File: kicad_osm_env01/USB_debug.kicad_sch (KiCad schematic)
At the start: 39 parts, among them J3 USB_B_Micro, Q2 SS8050, Q3 SS8050, U13 CP2102N-A02-GQFN24, U15 M74VHC1GT14DFT2G, U5 SP3003-02JTG

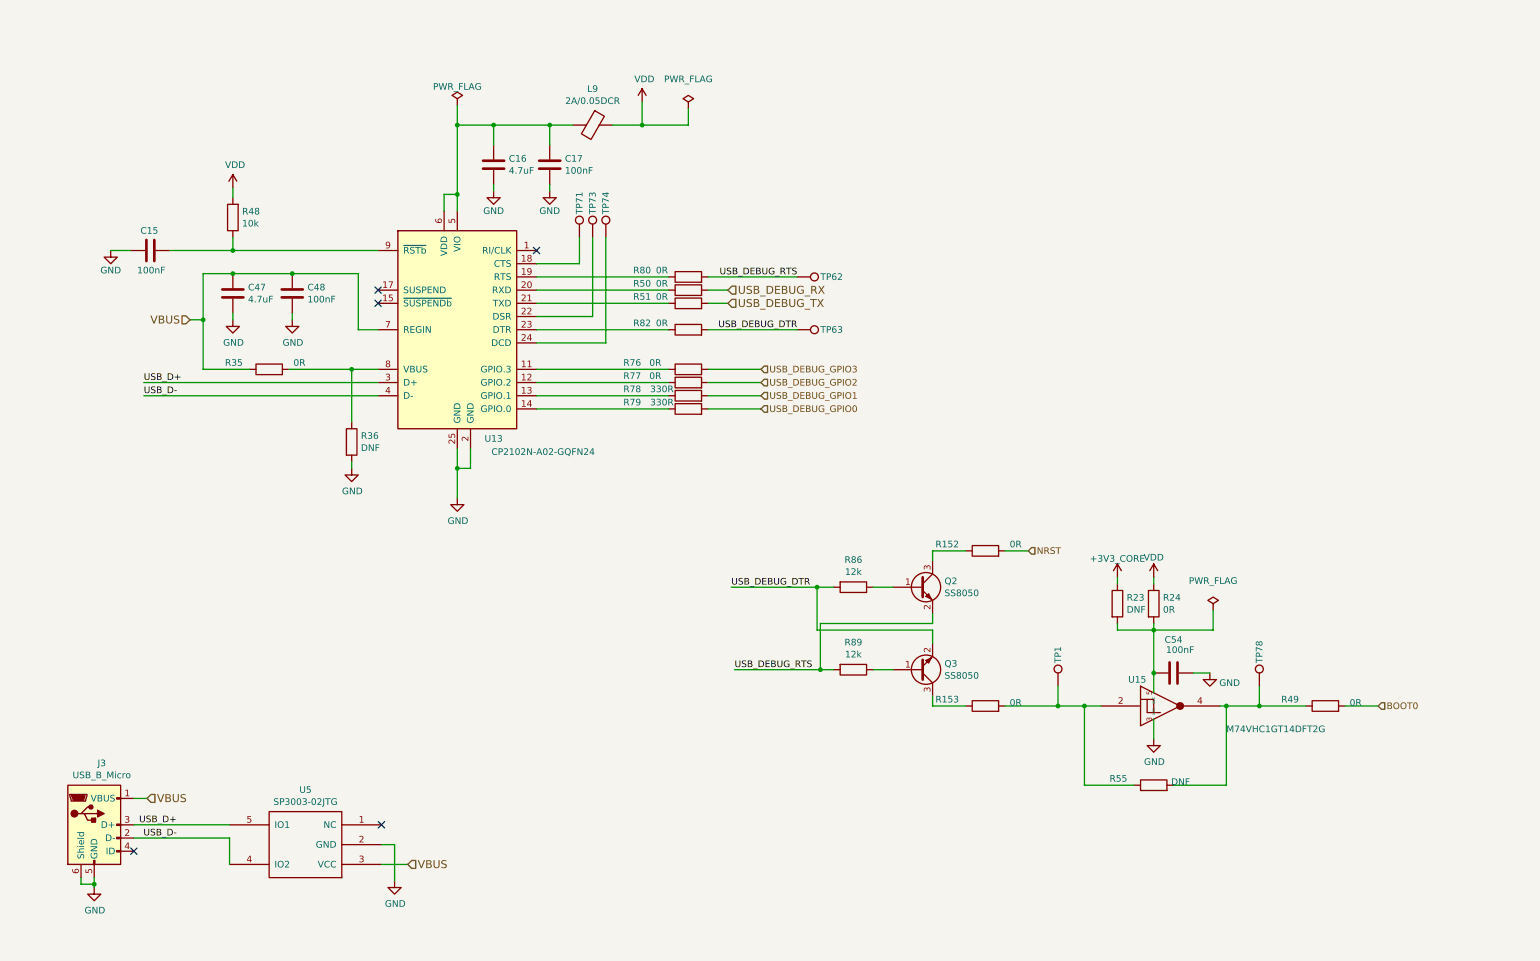
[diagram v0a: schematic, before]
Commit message: updated changes document with xnor power mod and updated schematics with mods so far for osm rev c
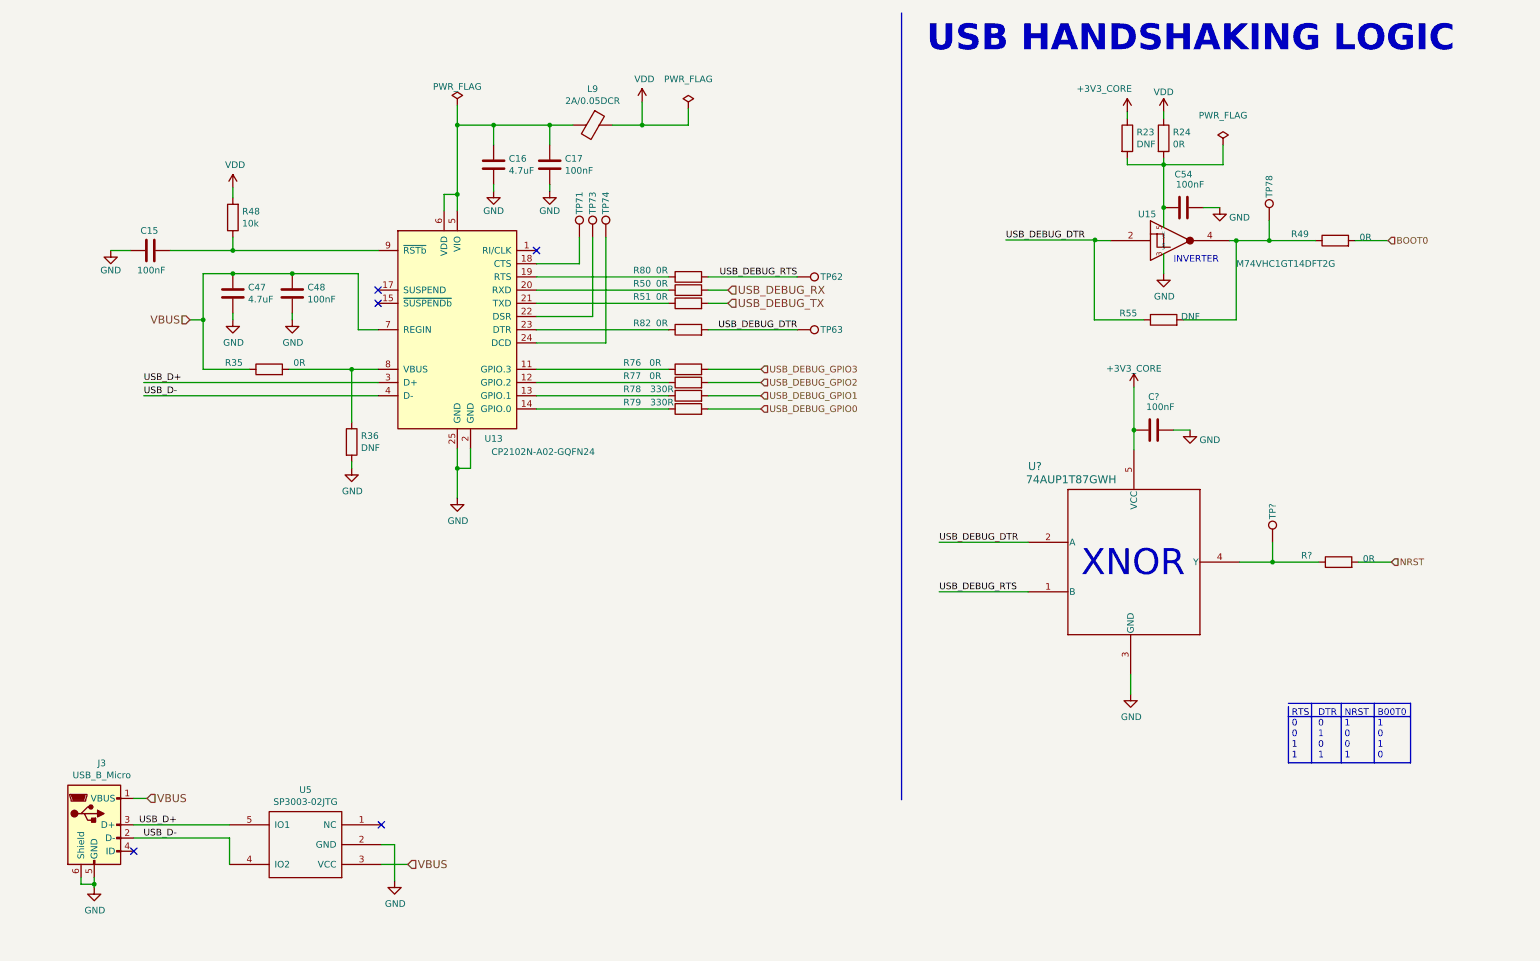
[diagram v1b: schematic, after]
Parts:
- removed Q2, Q3: SS8050, Package_TO_SOT_SMD:SOT-23, symbol Device:Q_NPN_BEC
- removed R152, R153: 0R, Resistor_SMD:R_0603_1608Metric, symbol Device:R
- removed R86, R89: 12k, Resistor_SMD:R_0603_1608Metric, symbol Device:R
- removed TP1: Test_Point, TestPoint:TestPoint_THTPad_D1.0mm_Drill0.5mm, symbol Connector:TestPoint
- added C?: 100nF, Capacitor_SMD:C_0402_1005Metric, symbol Device:C
- added R?: 0R, Resistor_SMD:R_0603_1608Metric, symbol Device:R
- added TP?: Test_Point, TestPoint:TestPoint_THTPad_D1.0mm_Drill0.5mm, symbol Connector:TestPoint
- added U?: 74AUP1T87GWH, symbol Devtank:74AUP1T87GWH
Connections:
- net +3V3_CORE: now also C?.2, U?.5 (VCC)
- net GND: now also C?.1, U?.3 (GND)
- net NRST: now also R?.2
- net USB_DEBUG_DTR: now also U?.2 (A)
- net USB_DEBUG_RTS: now also U?.1 (B)
- new net: R?.1, TP?.1, U?.4 (Y)
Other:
- note added: "B00T0 1 0 1 0"
- note added: "DTR 0 1 0 1"
- note added: "INVERTER"
- note added: "NRST 1 0 0 1"
- note added: "RTS 0 0 1 1"
- note added: "USB HANDSHAKING LOGIC"
- note added: "XNOR"
- moved on the sheet: C54, R23, R24, R49, R55, TP78, U15

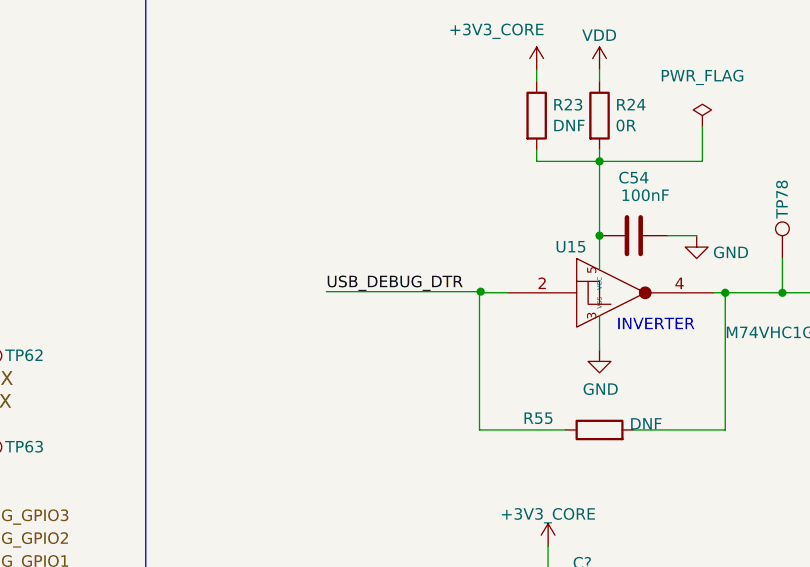
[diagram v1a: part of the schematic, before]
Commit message: Updated schematics with RevD V1.4 mods from CHANGES text file
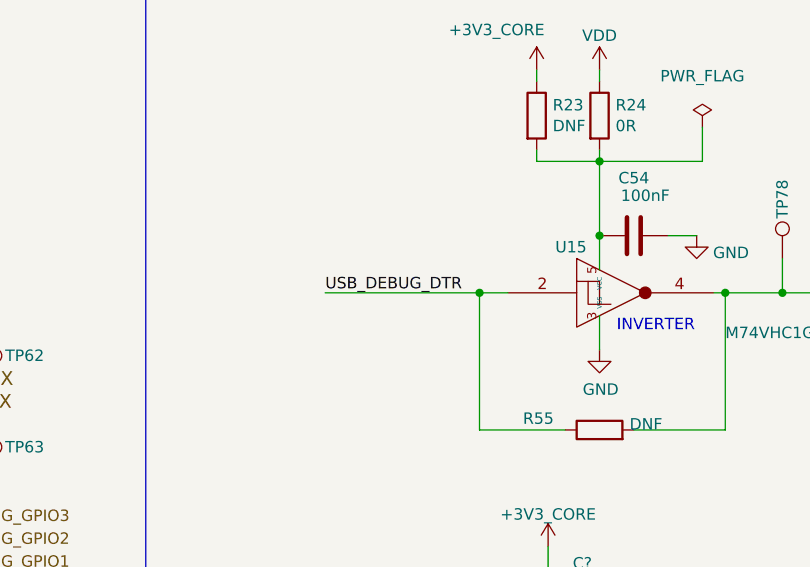
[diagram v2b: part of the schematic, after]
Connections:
- net USB_DEBUG_DTR: now also R55.1, U15.2

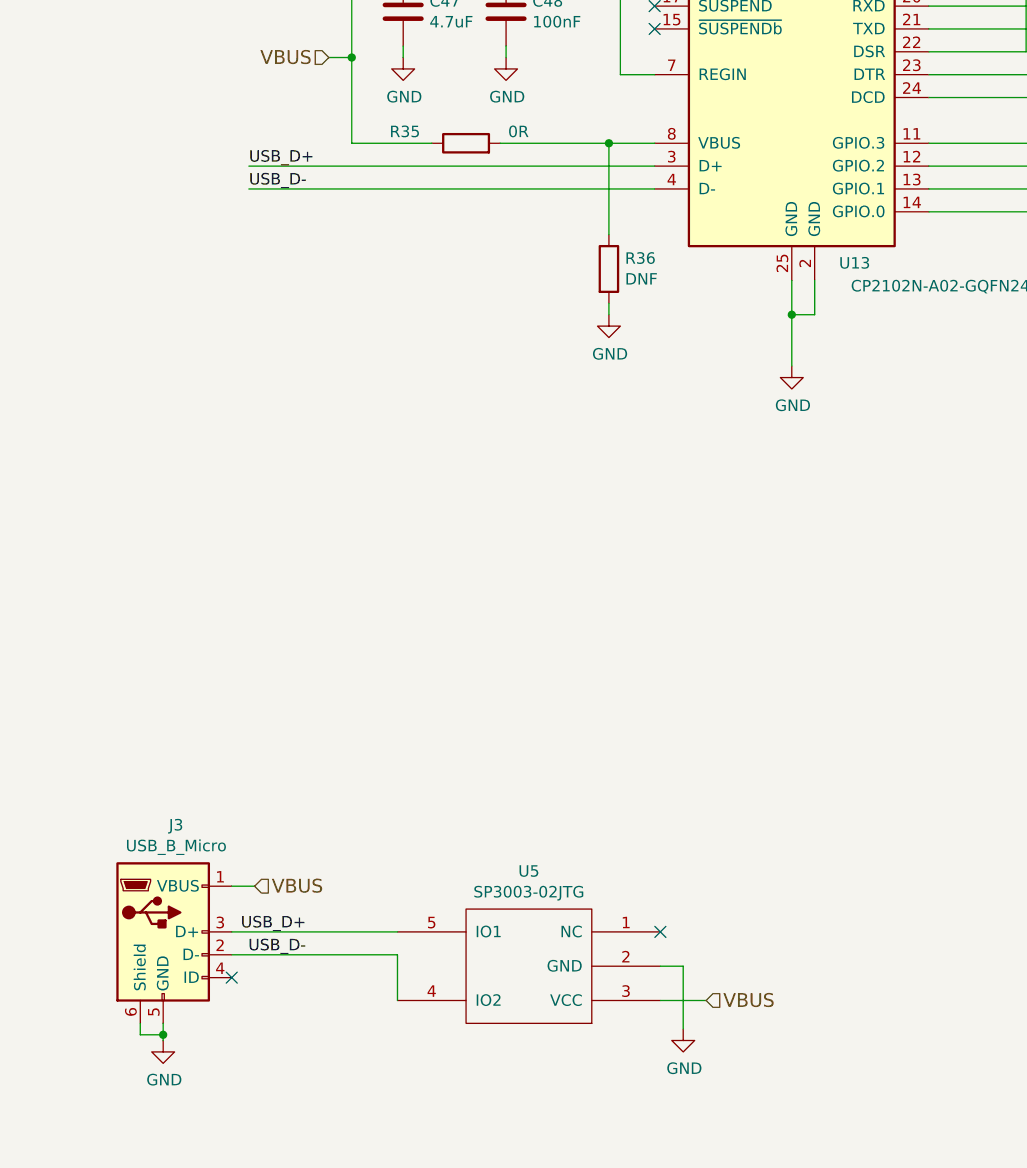
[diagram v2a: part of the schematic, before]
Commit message: added usb c connector to schematics
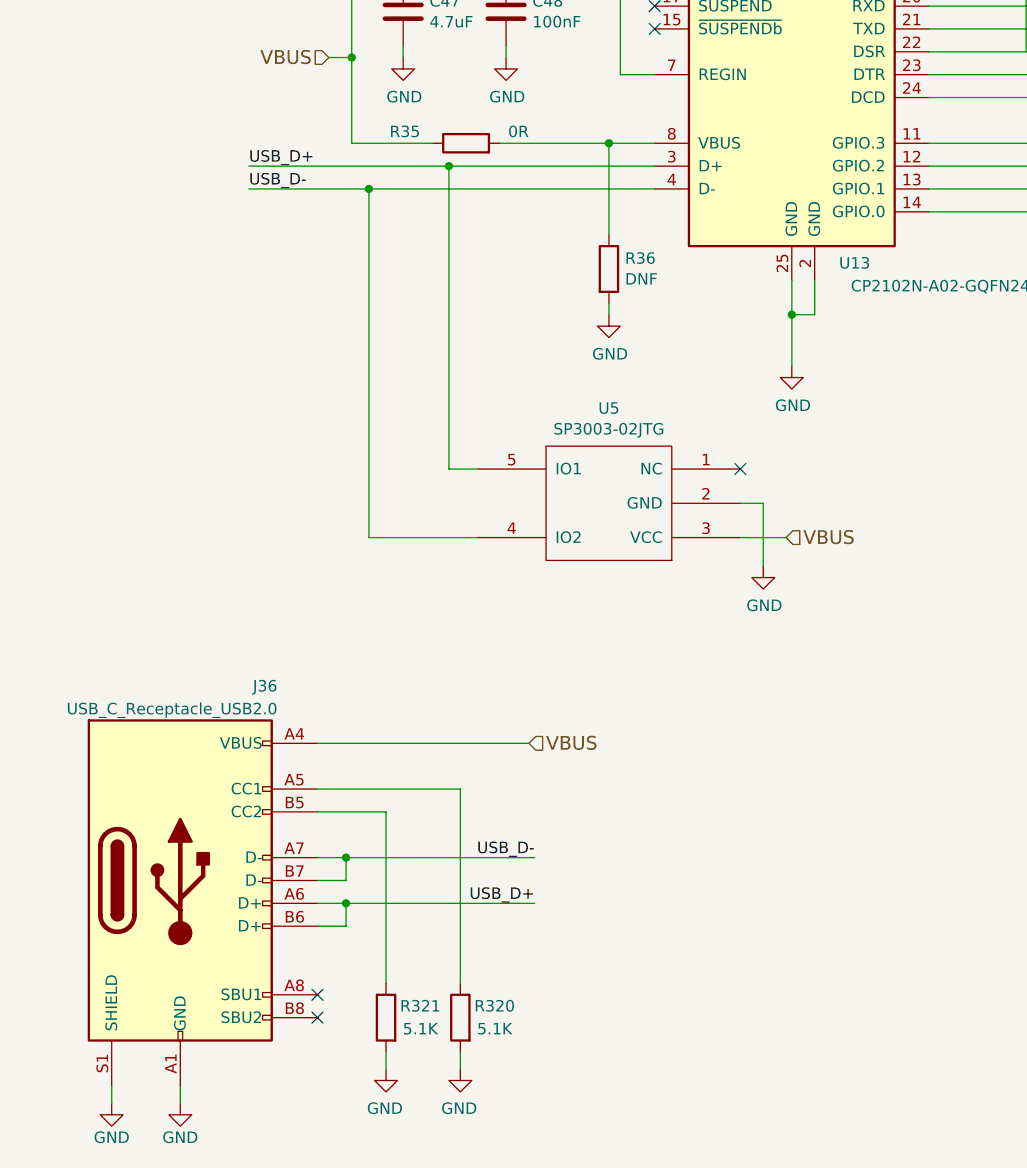
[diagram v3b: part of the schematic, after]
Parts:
- removed J3: USB_B_Micro, Devtank_PCB_lib:MOLEX_105017-0001_USB_B, symbol Connector:USB_B_Micro
- added J36: USB_C_Receptacle_USB2.0, Devtank_PCB_Lib:216989-0001_MOL, symbol Connector:USB_C_Receptacle_USB2.0
- added R320, R321: 5.1K, Resistor_SMD:R_0402_1005Metric, symbol Device:R
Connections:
- net GND: now also J36.A1 (GND), J36.A12 (GND), J36.B1 (GND), J36.B12 (GND), J36.S1 (SHIELD), R320.2, R321.2
- net USB_D+: now also J36.A6 (D+), J36.B6 (D+)
- net USB_D-: now also J36.A7 (D-), J36.B7 (D-)
- net VBUS: now also J36.A4 (VBUS), J36.A9 (VBUS), J36.B4 (VBUS), J36.B9 (VBUS)
- new net: J36.A5 (CC1), R320.1
- new net: J36.B5 (CC2), R321.1
- no-connect marks 5 -> 6
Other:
- moved on the sheet: U5
